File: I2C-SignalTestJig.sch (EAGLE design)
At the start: 49 parts, among them CON1 1x4, CON2 1x4, CON3 1x4, CON4 1x4, CON5 1x4, CON6 1x4, IC1 74LS139D, IC2 74LS139D, IC3 74LS139D, IC4 MCP23017SO

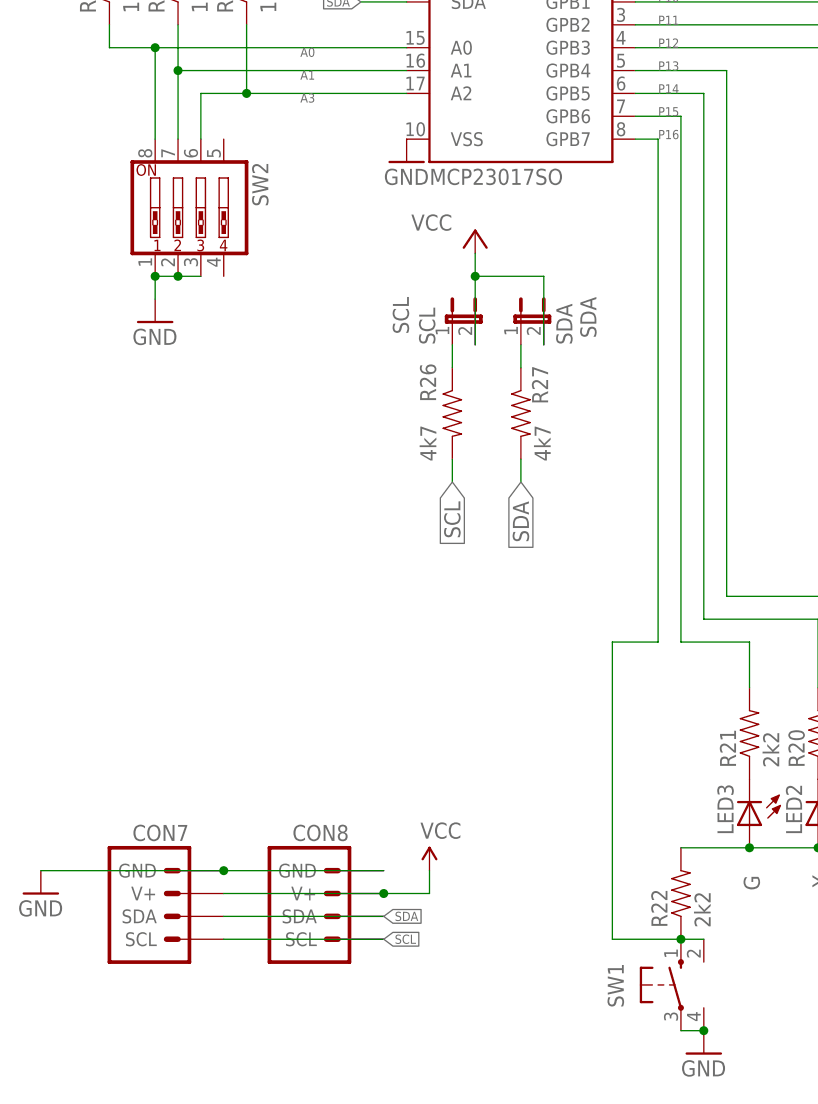
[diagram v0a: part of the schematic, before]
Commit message: added values for connectors
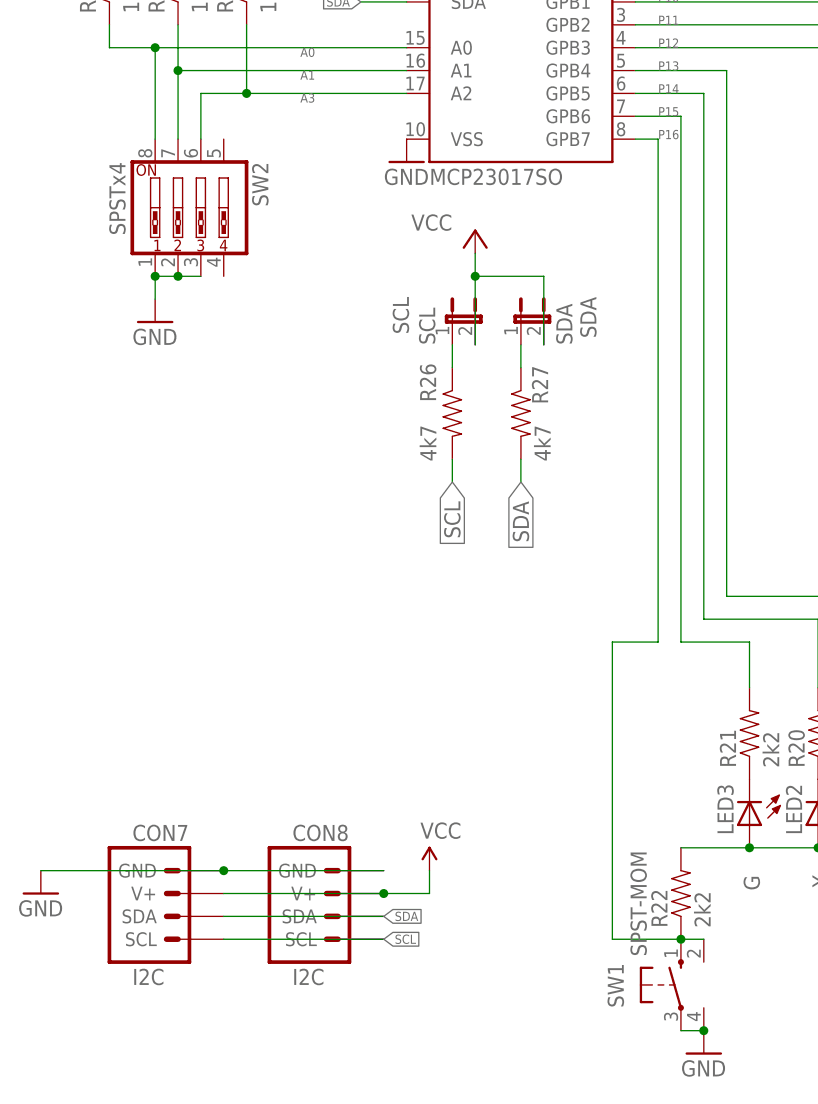
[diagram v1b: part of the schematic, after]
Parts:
- CON7, CON8: value (none) -> I2C
- SW1: value (none) -> SPST-MOM
- SW2: value (none) -> SPSTx4
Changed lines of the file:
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@@
 <part name="GND12" library="SparkFun" deviceset="GND" device=""/>
 <part name="IC4" library="SPCoast" deviceset="MCP23017" device="SO"/>
-<part name="CON7" library="SPCoast" deviceset="CONNECTOR-I2C" device="LEFT"/>
-<part name="CON8" library="SPCoast" deviceset="CONNECTOR-I2C" device="LEFT"/>
+<part name="CON7" library="SPCoast" deviceset="CONNECTOR-I2C" device="LEFT" value="I2C"/>
+<part name="CON8" library="SPCoast" deviceset="CONNECTOR-I2C" device="LEFT" value="I2C"/>
 <part name="GND1" library="SPCoast" deviceset="GND" device=""/>
 <part name="R26" library="SPCoast" deviceset="R*" device="0603-RES" value="4k7"/>
@@
 <part name="SCL" library="SPCoast" deviceset="JUMPER-2" device="PTH_LOCK" value="SCL"/>
 <part name="P+2" library="supply1" deviceset="VCC" device=""/>
-<part name="SW2" library="SPCoast" deviceset="SW_DIP-4" device=""/>
+<part name="SW2" library="SPCoast" deviceset="SW_DIP-4" device="" value="SPSTx4"/>
 <part name="R25" library="SPCoast" deviceset="R*" device="0603-RES" value="10K"/>
 <part name="R24" library="SPCoast" deviceset="R*" device="0603-RES" value="10K"/>
@@
 <part name="R20" library="SPCoast" deviceset="R*" device="0603-RES" value="2k2"/>
 <part name="R19" library="SPCoast" deviceset="R*" device="0603-RES" value="2k2"/>
-<part name="SW1" library="SPCoast" deviceset="SWITCH-(ON)" device="SMALLPADS"/>
+<part name="SW1" library="SPCoast" deviceset="SWITCH-(ON)" device="SMALLPADS" value="SPST-MOM"/>
 <part name="LED3" library="SPCoast" deviceset="LED*" device="0603-LED" value="G"/>
 <part name="LED2" library="SPCoast" deviceset="LED*" device="0603-LED" value="Y"/>

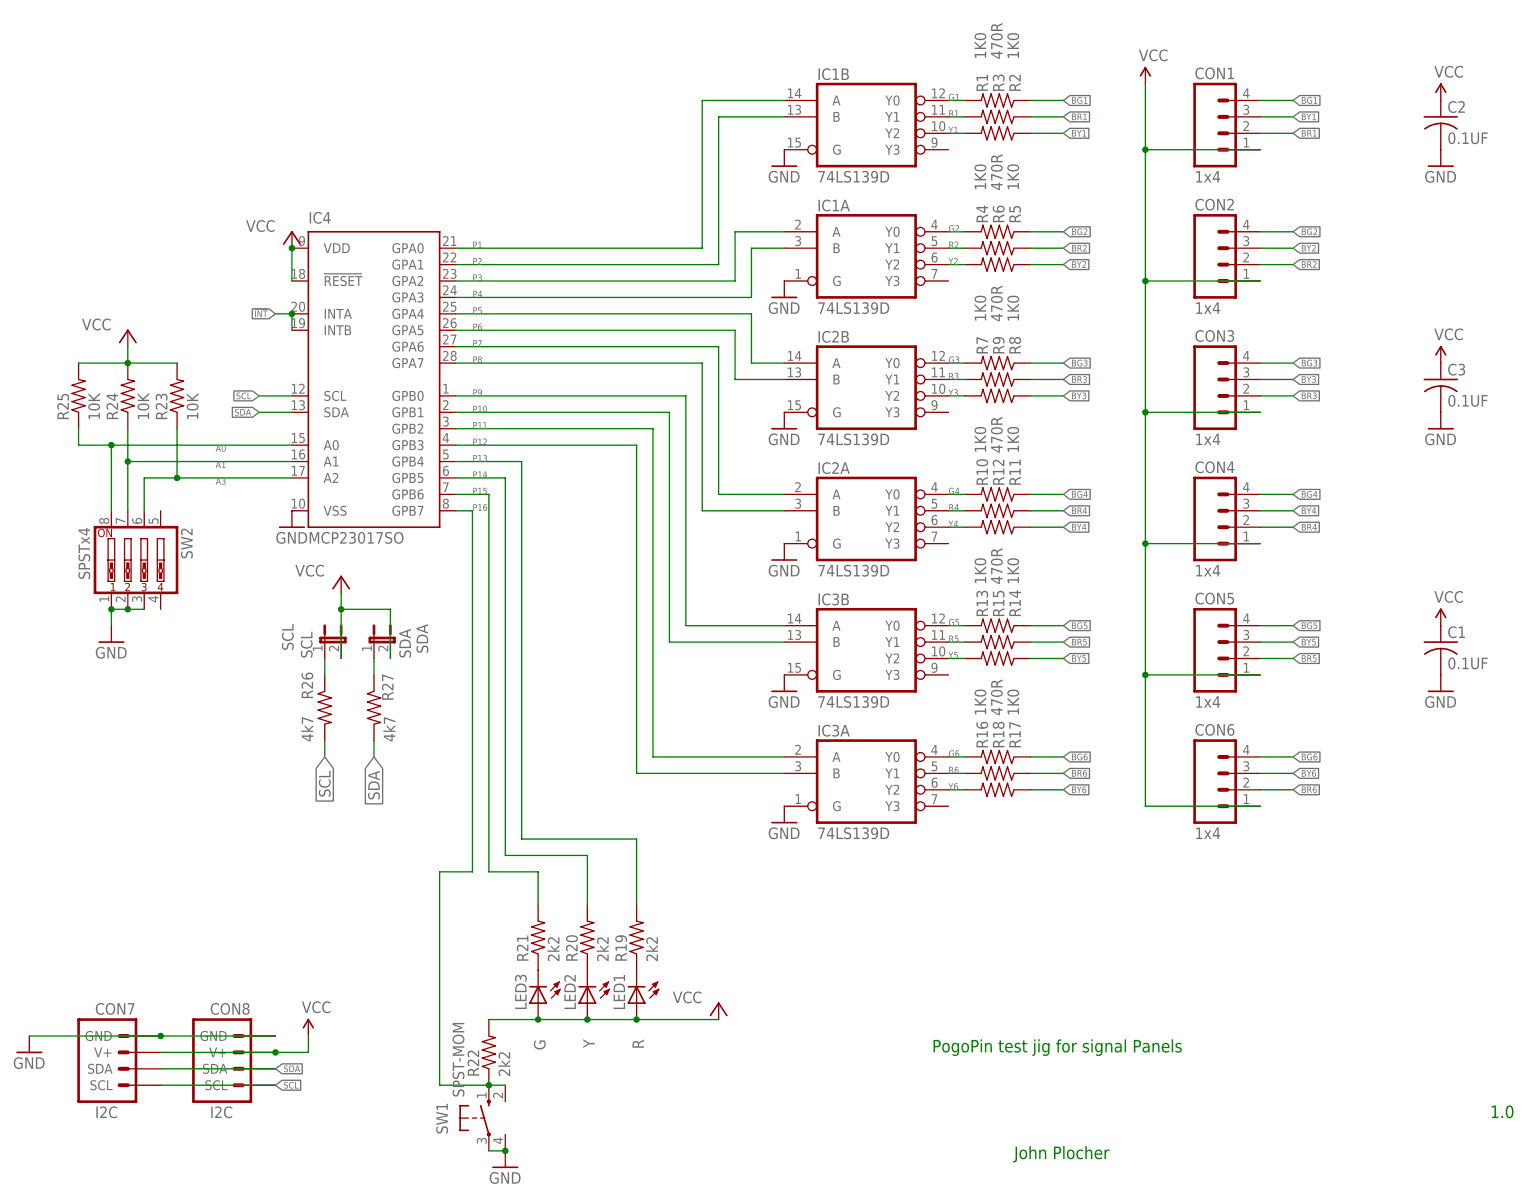
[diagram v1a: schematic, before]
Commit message: normalized values
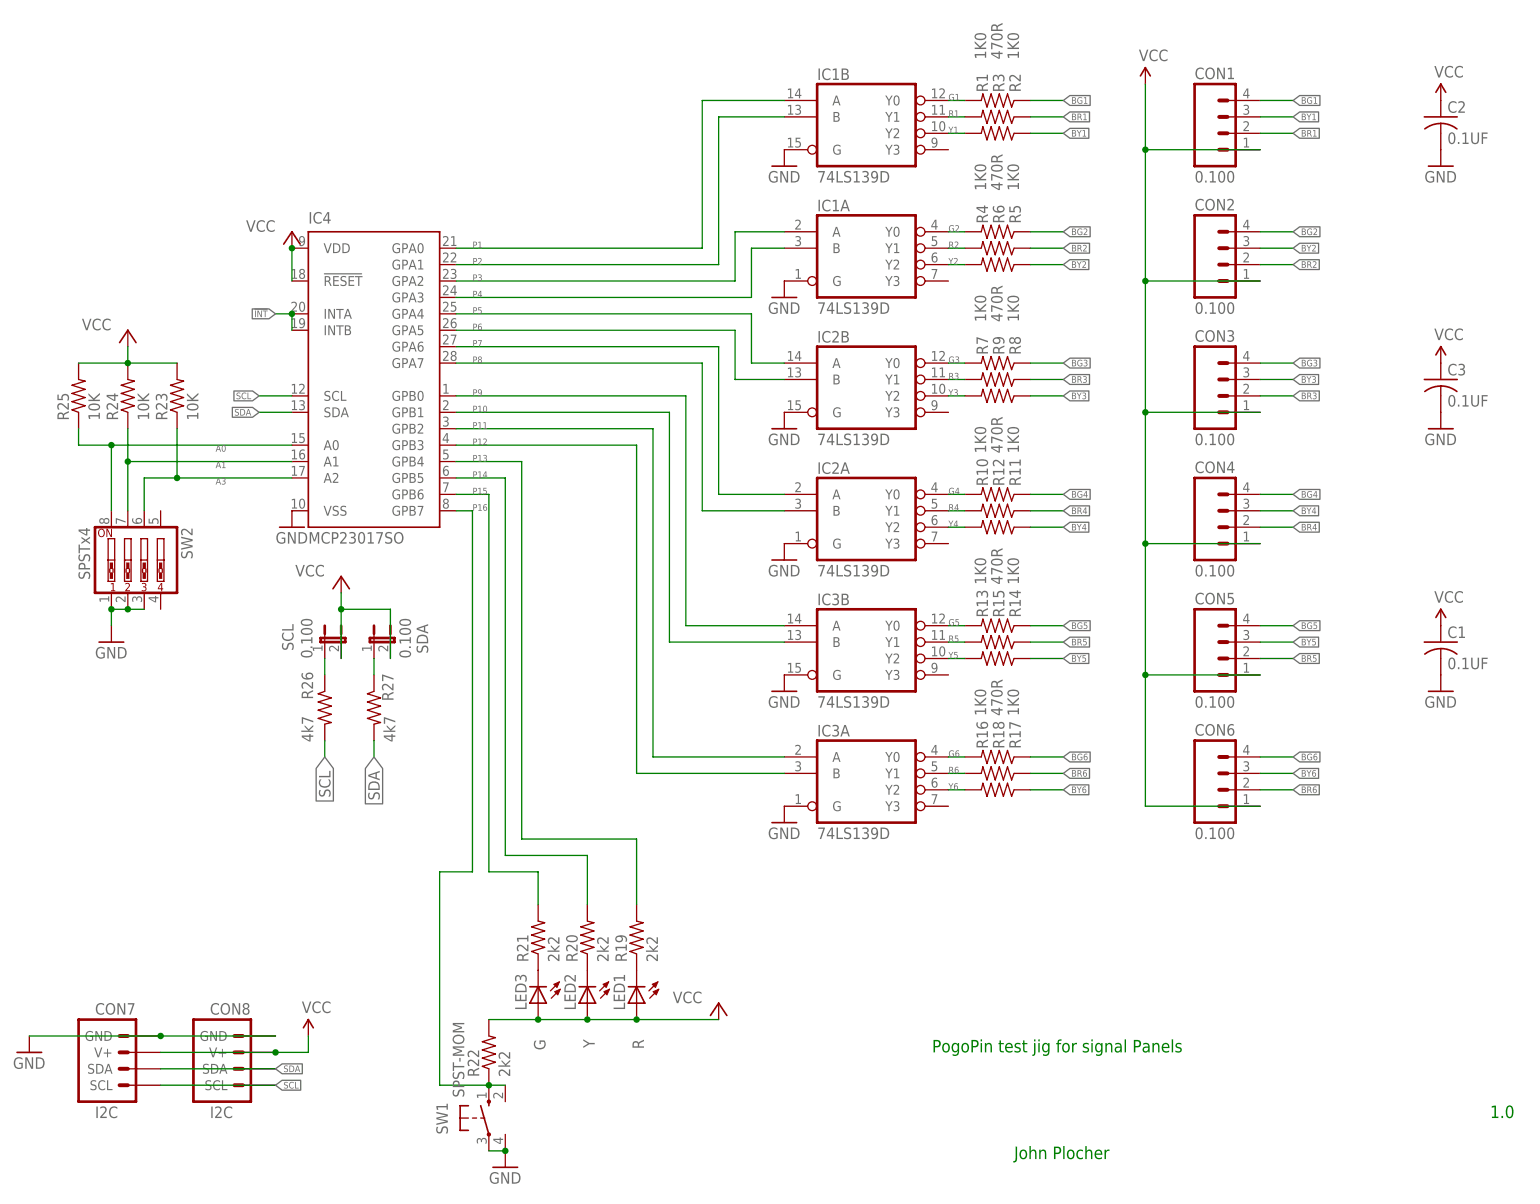
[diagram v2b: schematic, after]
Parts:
- CON1, CON2, CON3, CON4, CON5, CON6: value 1x4 -> 0.100
- SCL: value SCL -> 0.100
- SDA: value SDA -> 0.100
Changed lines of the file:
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@@
 <parts>
 <part name="FRAME1" library="SPCoast" deviceset="DOC-FRAME-LETTER" device=""/>
-<part name="CON1" library="SPCoast" deviceset="CONNECTOR-M04" device="LOCK" value="1x4"/>
-<part name="CON2" library="SPCoast" deviceset="CONNECTOR-M04" device="LOCK" value="1x4"/>
-<part name="CON3" library="SPCoast" deviceset="CONNECTOR-M04" device="LOCK" value="1x4"/>
-<part name="CON4" library="SPCoast" deviceset="CONNECTOR-M04" device="LOCK" value="1x4"/>
-<part name="CON5" library="SPCoast" deviceset="CONNECTOR-M04" device="LOCK" value="1x4"/>
-<part name="CON6" library="SPCoast" deviceset="CONNECTOR-M04" device="LOCK" value="1x4"/>
+<part name="CON1" library="SPCoast" deviceset="CONNECTOR-M04" device="LOCK" value="0.100"/>
+<part name="CON2" library="SPCoast" deviceset="CONNECTOR-M04" device="LOCK" value="0.100"/>
+<part name="CON3" library="SPCoast" deviceset="CONNECTOR-M04" device="LOCK" value="0.100"/>
+<part name="CON4" library="SPCoast" deviceset="CONNECTOR-M04" device="LOCK" value="0.100"/>
+<part name="CON5" library="SPCoast" deviceset="CONNECTOR-M04" device="LOCK" value="0.100"/>
+<part name="CON6" library="SPCoast" deviceset="CONNECTOR-M04" device="LOCK" value="0.100"/>
 <part name="IC1" library="SPCoast" deviceset="74*139" device="D" technology="LS"/>
 <part name="GND2" library="SparkFun" deviceset="GND" device=""/>
@@
 <part name="R26" library="SPCoast" deviceset="R*" device="0603-RES" value="4k7"/>
 <part name="R27" library="SPCoast" deviceset="R*" device="0603-RES" value="4k7"/>
-<part name="SDA" library="SPCoast" deviceset="JUMPER-2" device="PTH_LOCK" value="SDA"/>
-<part name="SCL" library="SPCoast" deviceset="JUMPER-2" device="PTH_LOCK" value="SCL"/>
+<part name="SDA" library="SPCoast" deviceset="JUMPER-2" device="PTH_LOCK" value="0.100"/>
+<part name="SCL" library="SPCoast" deviceset="JUMPER-2" device="PTH_LOCK" value="0.100"/>
 <part name="P+2" library="supply1" deviceset="VCC" device=""/>
 <part name="SW2" library="SPCoast" deviceset="SW_DIP-4" device="" value="SPSTx4"/>
